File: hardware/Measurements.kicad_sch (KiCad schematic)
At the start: 12 parts, among them U17 MCP6001-OT

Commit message: schematic override, just cuz
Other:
- sheet Isolated acu measurement ports: added HV_IN+, HV_IN-; removed HV_IN
- sheet Isolated car measurement ports: added HV_IN+, HV_IN-; removed HV_IN
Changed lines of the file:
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@@
     (stroke (width 0) (type default) (color 0 0 0 0))
   )
-  (wire (pts (xy 103.505 56.515) (xy 106.045 56.515))
+  (wire (pts (xy 103.505 41.275) (xy 106.045 41.275))
     (stroke (width 0) (type default) (color 0 0 0 0))
   )
   (wire (pts (xy 219.075 91.44) (xy 219.075 92.71))
+    (stroke (width 0) (type default) (color 0 0 0 0))
+  )
+  (wire (pts (xy 74.295 43.815) (xy 76.835 43.815))
     (stroke (width 0) (type default) (color 0 0 0 0))
   )
@@
     (stroke (width 0) (type default) (color 0 0 0 0))
   )
-  (wire (pts (xy 74.295 56.515) (xy 76.835 56.515))
+  (wire (pts (xy 74.295 76.835) (xy 76.835 76.835))
+    (stroke (width 0) (type default) (color 0 0 0 0))
+  )
+  (wire (pts (xy 74.295 41.275) (xy 76.835 41.275))
     (stroke (width 0) (type default) (color 0 0 0 0))
   )
@@
     (effects (font (size 1.27 1.27)) (justify left bottom))
   )
-  (global_label "HV_CAR_VOLTAGE" (shape input) (at 74.295 74.295 180) (fields_autoplaced)
+  (global_label "HV_CAR+" (shape input) (at 74.295 74.295 180) (fields_autoplaced)
     (effects (font (size 1.27 1.27)) (justify right))
-    (property "Intersheet References" "${INTERSHEET_REFS}" (id 0) (at 56.0656 74.2156 0)
+    (property "Intersheet References" "${INTERSHEET_REFS}" (id 0) (at 63.3832 74.2156 0)
       (effects (font (size 1.27 1.27)) (justify right) hide)
     )
@@
     )
   )
-  (global_label "HV_ACU_VOLTAGE" (shape input) (at 74.295 56.515 180) (fields_autoplaced)
+  (global_label "HV_ACU-" (shape input) (at 74.295 43.815 180) (fields_autoplaced)
     (effects (font (size 1.27 1.27)) (justify right))
-    (property "Intersheet References" "${INTERSHEET_REFS}" (id 0) (at 56.0051 56.4356 0)
+    (property "Intersheet References" "${INTERSHEET_REFS}" (id 0) (at 63.3227 43.7356 0)
+      (effects (font (size 1.27 1.27)) (justify right) hide)
+    )
+  )
+  (global_label "HV_ACU+" (shape input) (at 74.295 41.275 180) (fields_autoplaced)
+    (effects (font (size 1.27 1.27)) (justify right))
+    (property "Intersheet References" "${INTERSHEET_REFS}" (id 0) (at 63.3227 41.1956 0)
       (effects (font (size 1.27 1.27)) (justify right) hide)
     )
@@
     )
   )
-  (hierarchical_label "ACU_V_ADC" (shape input) (at 106.045 56.515 0)
+  (global_label "HV_CAR-" (shape input) (at 74.295 76.835 180) (fields_autoplaced)
+    (effects (font (size 1.27 1.27)) (justify right))
+    (property "Intersheet References" "${INTERSHEET_REFS}" (id 0) (at 63.3832 76.7556 0)
+      (effects (font (size 1.27 1.27)) (justify right) hide)
+    )
+  )
+  (hierarchical_label "ACU_V_ADC" (shape output) (at 106.045 41.275 0)
     (effects (font (size 1.27 1.27)) (justify left))
   )
-  (hierarchical_label "CAR_V_ADC" (shape input) (at 106.045 74.295 0)
+  (hierarchical_label "CAR_V_ADC" (shape output) (at 106.045 74.295 0)
     (effects (font (size 1.27 1.27)) (justify left))
   )
-  (hierarchical_label "SENSOR_SIGNAL_MCU" (shape input) (at 114.935 161.29 0)
+  (hierarchical_label "SENSOR_SIGNAL_MCU" (shape output) (at 114.935 161.29 0)
     (effects (font (size 1.27 1.27)) (justify left))
   )
@@
     (pin "2")
   )
-  (sheet (at 76.835 72.39) (size 26.67 3.81) (fields_autoplaced)
+  (sheet (at 76.835 72.39) (size 26.67 6.35) (fields_autoplaced)
     (stroke (width 0.1524) (type solid) (color 0 0 0 0))
     (fill (color 0 0 0 0.0000))
@@
       (effects (font (size 1.27 1.27)) (justify left bottom))
     )
-    (property "Sheet file" "IsolatedMeasurement.kicad_sch" (id 1) (at 76.835 76.7846 0)
+    (property "Sheet file" "IsolatedMeasurement.kicad_sch" (id 1) (at 76.835 79.3246 0)
       (effects (font (size 1.27 1.27)) (justify left top))
     )
-    (pin "HV_IN" input (at 76.835 74.295 180)
-      (effects (font (size 1.27 1.27)) (justify left))
-    )
-    (pin "LV_OUT" input (at 103.505 74.295 0)
+    (pin "HV_IN+" input (at 76.835 74.295 180)
+      (effects (font (size 1.27 1.27)) (justify left))
+    )
+    (pin "LV_OUT" output (at 103.505 74.295 0)
       (effects (font (size 1.27 1.27)) (justify right))
     )
-  )
-  (sheet (at 76.835 54.61) (size 26.67 3.81) (fields_autoplaced)
+    (pin "HV_IN-" input (at 76.835 76.835 180)
+      (effects (font (size 1.27 1.27)) (justify left))
+    )
+  )
+  (sheet (at 76.835 39.37) (size 26.67 6.35) (fields_autoplaced)
     (stroke (width 0.1524) (type solid) (color 0 0 0 0))
     (fill (color 0 0 0 0.0000))
-    (property "Sheet name" "Isolated acu measurement" (id 0) (at 76.835 53.8984 0)
+    (property "Sheet name" "Isolated acu measurement" (id 0) (at 76.835 38.6584 0)
       (effects (font (size 1.27 1.27)) (justify left bottom))
     )
-    (property "Sheet file" "IsolatedMeasurement.kicad_sch" (id 1) (at 76.835 59.0046 0)
+    (property "Sheet file" "IsolatedMeasurement.kicad_sch" (id 1) (at 76.835 46.3046 0)
       (effects (font (size 1.27 1.27)) (justify left top))
     )
-    (pin "HV_IN" input (at 76.835 56.515 180)
-      (effects (font (size 1.27 1.27)) (justify left))
-    )
-    (pin "LV_OUT" input (at 103.505 56.515 0)
+    (pin "HV_IN+" input (at 76.835 41.275 180)
+      (effects (font (size 1.27 1.27)) (justify left))
+    )
+    (pin "LV_OUT" output (at 103.505 41.275 0)
       (effects (font (size 1.27 1.27)) (justify right))
     )
-  )
+    (pin "HV_IN-" input (at 76.835 43.815 180)
+      (effects (font (size 1.27 1.27)) (justify left))
+    )
+  )

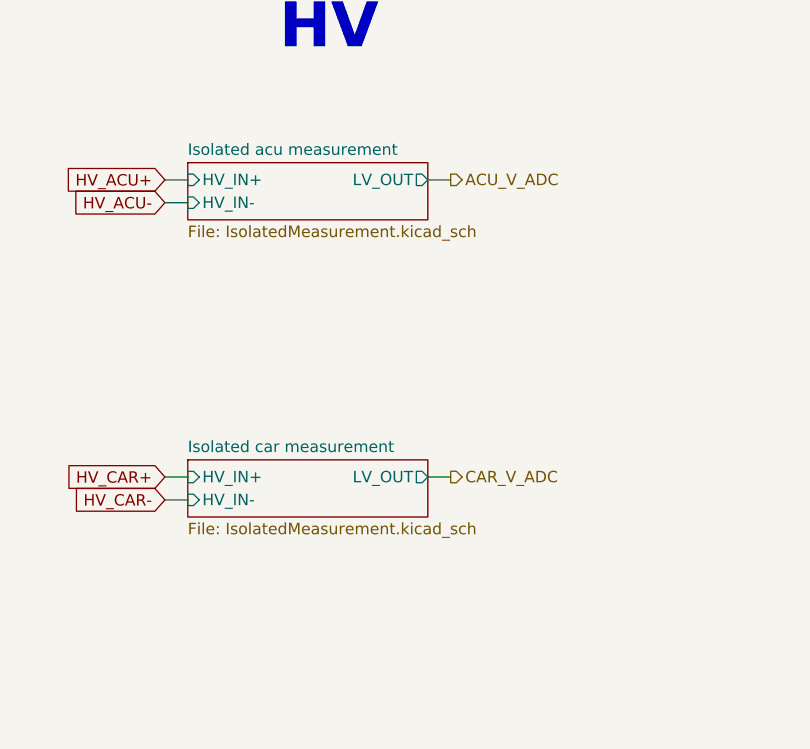
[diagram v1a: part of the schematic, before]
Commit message: changed HV measurements from isolated opamp to isolated ADC with isolated spi communication, changed safety laatching from mosfet back to relay
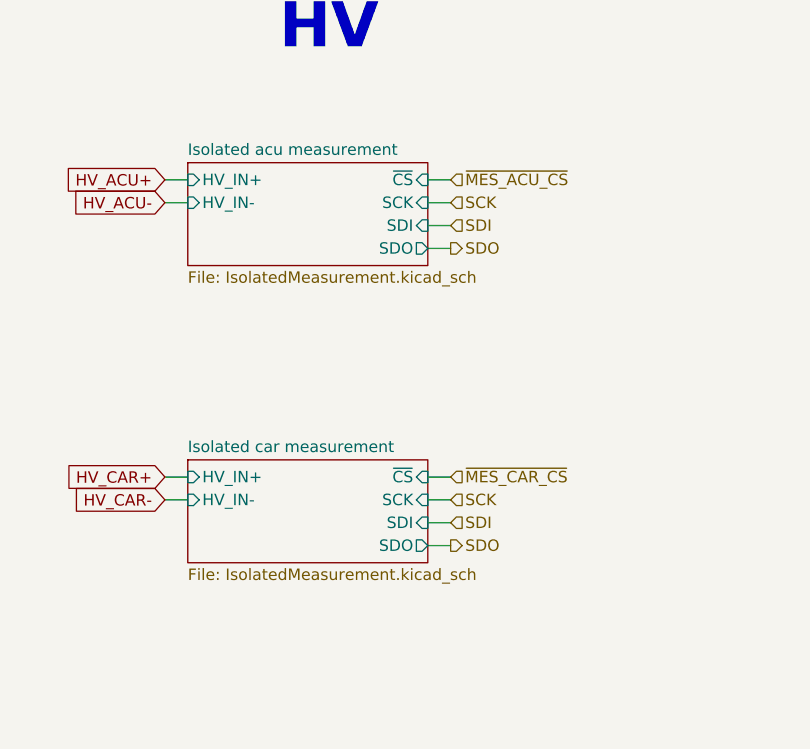
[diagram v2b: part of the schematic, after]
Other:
- sheet Isolated acu measurement ports: added SCK, SDI, SDO, ~{CS}; removed LV_OUT
- sheet Isolated car measurement ports: added SCK, SDI, SDO, ~{CS}; removed LV_OUT
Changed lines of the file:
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@@
-    (stroke (width 0) (type default) (color 0 0 0 0))
-  )
-  (wire (pts (xy 103.505 41.275) (xy 106.045 41.275))
     (stroke (width 0) (type default) (color 0 0 0 0))
   )
@@
   )
   (wire (pts (xy 103.505 161.29) (xy 104.775 161.29))
+    (stroke (width 0) (type default) (color 0 0 0 0))
+  )
+  (wire (pts (xy 103.505 81.915) (xy 106.045 81.915))
     (stroke (width 0) (type default) (color 0 0 0 0))
   )
@@
     (stroke (width 1) (type default) (color 132 0 0 1))
   )
+  (wire (pts (xy 103.505 41.275) (xy 106.045 41.275))
+    (stroke (width 0) (type default) (color 0 0 0 0))
+  )
+  (wire (pts (xy 103.505 43.815) (xy 106.045 43.815))
+    (stroke (width 0) (type default) (color 0 0 0 0))
+  )
   (wire (pts (xy 226.695 83.82) (xy 226.695 86.36))
     (stroke (width 0) (type default) (color 0 0 0 0))
@@
     (stroke (width 0) (type default) (color 0 0 0 0))
   )
+  (wire (pts (xy 94.615 152.4) (xy 93.345 152.4))
+    (stroke (width 0) (type default) (color 0 0 0 0))
+  )
+  (wire (pts (xy 103.505 76.835) (xy 106.045 76.835))
+    (stroke (width 0) (type default) (color 0 0 0 0))
+  )
+  (wire (pts (xy 93.345 152.4) (xy 93.345 153.67))
+    (stroke (width 0) (type default) (color 0 0 0 0))
+  )
+  (wire (pts (xy 103.505 46.355) (xy 106.045 46.355))
+    (stroke (width 0) (type default) (color 0 0 0 0))
+  )
+  (wire (pts (xy 62.23 168.91) (xy 69.85 168.91))
+    (stroke (width 0) (type default) (color 0 0 0 0))
+  )
   (wire (pts (xy 103.505 74.295) (xy 106.045 74.295))
     (stroke (width 0) (type default) (color 0 0 0 0))
   )
-  (wire (pts (xy 94.615 152.4) (xy 93.345 152.4))
-    (stroke (width 0) (type default) (color 0 0 0 0))
-  )
-  (wire (pts (xy 93.345 152.4) (xy 93.345 153.67))
-    (stroke (width 0) (type default) (color 0 0 0 0))
-  )
-  (wire (pts (xy 62.23 168.91) (xy 69.85 168.91))
-    (stroke (width 0) (type default) (color 0 0 0 0))
-  )
   (wire (pts (xy 219.075 92.71) (xy 219.075 99.06))
+    (stroke (width 0) (type default) (color 0 0 0 0))
+  )
+  (wire (pts (xy 103.505 79.375) (xy 106.045 79.375))
+    (stroke (width 0) (type default) (color 0 0 0 0))
+  )
+  (wire (pts (xy 103.505 48.895) (xy 106.045 48.895))
     (stroke (width 0) (type default) (color 0 0 0 0))
   )
@@
     )
   )
-  (hierarchical_label "ACU_V_ADC" (shape output) (at 106.045 41.275 0)
-    (effects (font (size 1.27 1.27)) (justify left))
-  )
-  (hierarchical_label "CAR_V_ADC" (shape output) (at 106.045 74.295 0)
+  (hierarchical_label "~{MES_ACU_CS}" (shape input) (at 106.045 41.275 0)
+    (effects (font (size 1.27 1.27)) (justify left))
+  )
+  (hierarchical_label "SDO" (shape output) (at 106.045 48.895 0)
+    (effects (font (size 1.27 1.27)) (justify left))
+  )
+  (hierarchical_label "~{MES_CAR_CS}" (shape input) (at 106.045 74.295 0)
+    (effects (font (size 1.27 1.27)) (justify left))
+  )
+  (hierarchical_label "SDI" (shape input) (at 106.045 79.375 0)
+    (effects (font (size 1.27 1.27)) (justify left))
+  )
+  (hierarchical_label "SDI" (shape input) (at 106.045 46.355 0)
+    (effects (font (size 1.27 1.27)) (justify left))
+  )
+  (hierarchical_label "SDO" (shape output) (at 106.045 81.915 0)
+    (effects (font (size 1.27 1.27)) (justify left))
+  )
+  (hierarchical_label "SCK" (shape input) (at 106.045 76.835 0)
     (effects (font (size 1.27 1.27)) (justify left))
   )
   (hierarchical_label "SENSOR_SIGNAL_MCU" (shape output) (at 114.935 161.29 0)
+    (effects (font (size 1.27 1.27)) (justify left))
+  )
+  (hierarchical_label "SCK" (shape input) (at 106.045 43.815 0)
     (effects (font (size 1.27 1.27)) (justify left))
   )
@@
     (pin "2")
   )
-  (sheet (at 76.835 72.39) (size 26.67 6.35) (fields_autoplaced)
+  (sheet (at 76.835 72.39) (size 26.67 11.43) (fields_autoplaced)
     (stroke (width 0.1524) (type solid) (color 0 0 0 0))
     (fill (color 0 0 0 0.0000))
@@
       (effects (font (size 1.27 1.27)) (justify left bottom))
     )
-    (property "Sheet file" "IsolatedMeasurement.kicad_sch" (id 1) (at 76.835 79.3246 0)
+    (property "Sheet file" "IsolatedMeasurement.kicad_sch" (id 1) (at 76.835 84.4046 0)
       (effects (font (size 1.27 1.27)) (justify left top))
     )
@@
       (effects (font (size 1.27 1.27)) (justify left))
     )
-    (pin "LV_OUT" output (at 103.505 74.295 0)
-      (effects (font (size 1.27 1.27)) (justify right))
-    )
     (pin "HV_IN-" input (at 76.835 76.835 180)
       (effects (font (size 1.27 1.27)) (justify left))
     )
-  )
-  (sheet (at 76.835 39.37) (size 26.67 6.35) (fields_autoplaced)
+    (pin "~{CS}" input (at 103.505 74.295 0)
+      (effects (font (size 1.27 1.27)) (justify right))
+    )
+    (pin "SCK" input (at 103.505 76.835 0)
+      (effects (font (size 1.27 1.27)) (justify right))
+    )
+    (pin "SDI" input (at 103.505 79.375 0)
+      (effects (font (size 1.27 1.27)) (justify right))
+    )
+    (pin "SDO" output (at 103.505 81.915 0)
+      (effects (font (size 1.27 1.27)) (justify right))
+    )
+  )
+  (sheet (at 76.835 39.37) (size 26.67 11.43) (fields_autoplaced)
     (stroke (width 0.1524) (type solid) (color 0 0 0 0))
     (fill (color 0 0 0 0.0000))
@@
       (effects (font (size 1.27 1.27)) (justify left bottom))
     )
-    (property "Sheet file" "IsolatedMeasurement.kicad_sch" (id 1) (at 76.835 46.3046 0)
+    (property "Sheet file" "IsolatedMeasurement.kicad_sch" (id 1) (at 76.835 51.3846 0)
       (effects (font (size 1.27 1.27)) (justify left top))
     )
@@
       (effects (font (size 1.27 1.27)) (justify left))
     )
-    (pin "LV_OUT" output (at 103.505 41.275 0)
-      (effects (font (size 1.27 1.27)) (justify right))
-    )
     (pin "HV_IN-" input (at 76.835 43.815 180)
       (effects (font (size 1.27 1.27)) (justify left))
     )
-  )
+    (pin "~{CS}" input (at 103.505 41.275 0)
+      (effects (font (size 1.27 1.27)) (justify right))
+    )
+    (pin "SCK" input (at 103.505 43.815 0)
+      (effects (font (size 1.27 1.27)) (justify right))
+    )
+    (pin "SDI" input (at 103.505 46.355 0)
+      (effects (font (size 1.27 1.27)) (justify right))
+    )
+    (pin "SDO" output (at 103.505 48.895 0)
+      (effects (font (size 1.27 1.27)) (justify right))
+    )
+  )

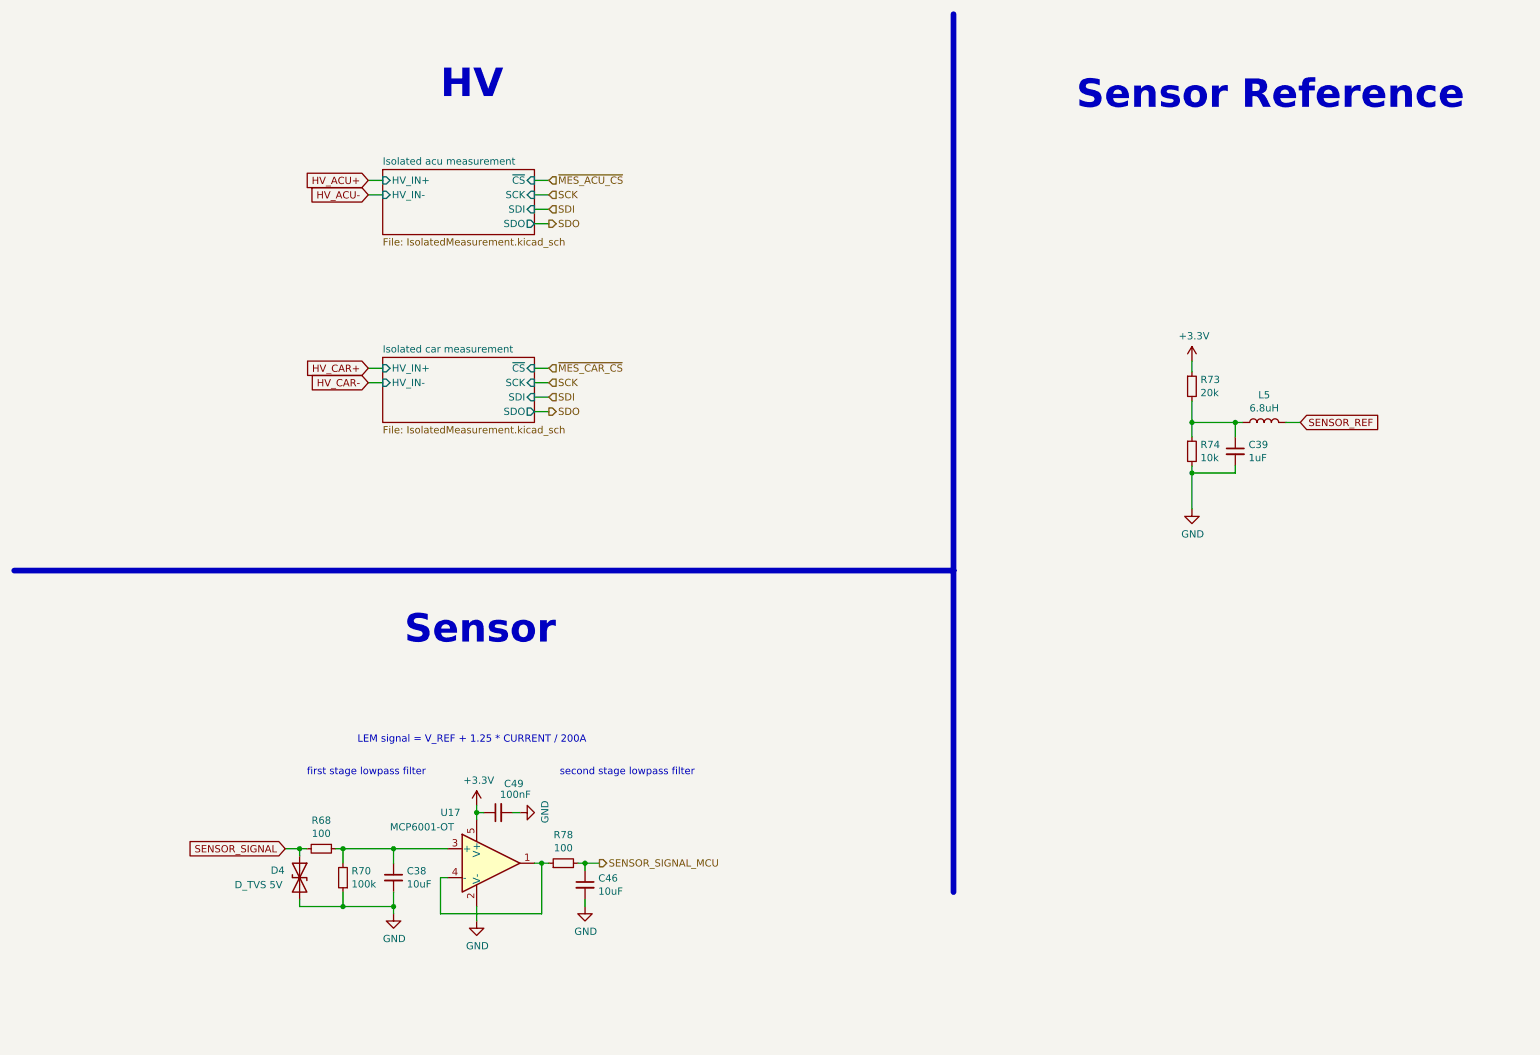
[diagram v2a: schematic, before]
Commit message: changed the 1V voltage ref made from RL circuit to low noise, 0.1% error 1.024 V ref gen, and changed the opamp used for current sensor feedback filtration to a high precision low drift opamp
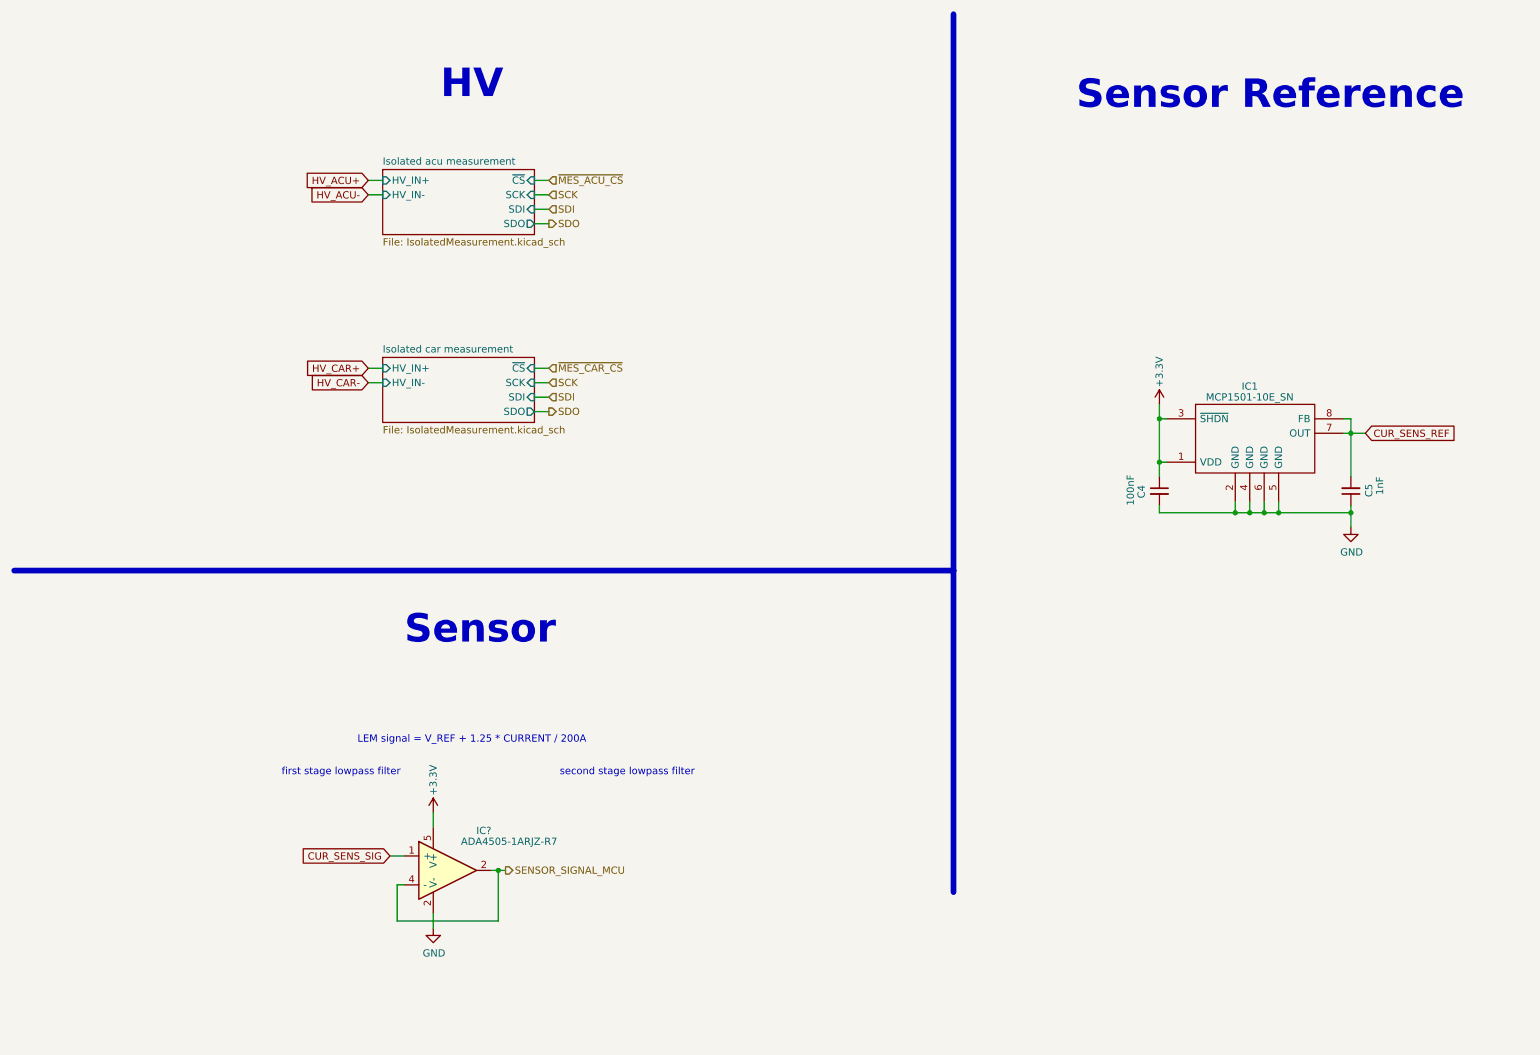
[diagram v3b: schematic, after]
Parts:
- removed C38, C46: 10uF, Capacitor_SMD:C_0603_1608Metric, symbol Device:C_Small
- removed C39: 1uF, Capacitor_SMD:C_0603_1608Metric, symbol Device:C_Small
- removed C49: 100nF, Capacitor_SMD:C_0603_1608Metric, symbol Device:C_Small
- removed D4: D_TVS 5V, Diode_SMD:D_SMA, symbol Device:D_TVS
- removed L5: 6.8uH, Inductor_SMD:L_1206_3216Metric, symbol Device:L
- removed R68, R78: 100, Resistor_SMD:R_0603_1608Metric, symbol Device:R_Small
- removed R70: 100k, Resistor_SMD:R_0603_1608Metric, symbol Device:R_Small
- removed R73: 20k, Resistor_SMD:R_0603_1608Metric, symbol Device:R_Small
- removed R74: 10k, Resistor_SMD:R_0603_1608Metric, symbol Device:R_Small
- removed U17: MCP6001-OT, Package_TO_SOT_SMD:SOT-23-5, symbol Amplifier_Operational:MCP6001-OT
- added C4: 100nF, Capacitor_SMD:C_0603_1608Metric, symbol Device:C_Small
- added C5: 1nF, Capacitor_SMD:C_0603_1608Metric, symbol Device:C_Small
- added IC1: MCP1501-10E_SN, SOIC127P600X175-8N, symbol MCP1501-10E_SN:MCP1501-10E_SN
- added IC?: ADA4505-1ARJZ-R7, SOT95P280X145-5N, symbol ADA4505-1ARJZ-R7:ADA4505-1ARJZ-R7
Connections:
- net +3V3: now also C4.1, IC1.1 (VDD), IC1.3 (~{SHDN}), IC?.5 (V+)
- net GND: now also C4.2, C5.1, IC1.2 (GND), IC1.4 (GND), IC1.5 (GND), IC1.6 (GND), IC?.2
- net SENSOR_SIGNAL_MCU: now also IC?.2, IC?.4 (-)
- new net CUR_SENS_REF: C5.2, IC1.7 (OUT), IC1.8 (FB)
- new net CUR_SENS_SIG: IC?.1 (NC)
